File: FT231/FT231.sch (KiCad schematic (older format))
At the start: 19 parts, among them J1 USB_B_Micro, J2 Conn_01x03, J3 Conn_01x03, J4 Conn_01x06, U1 FT231XQ

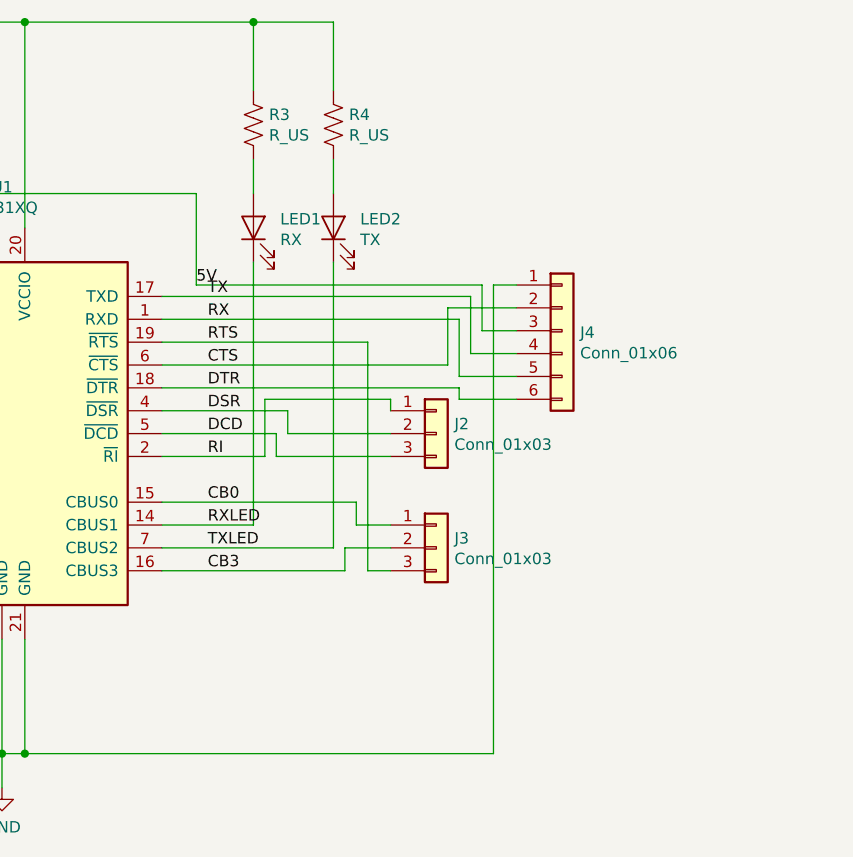
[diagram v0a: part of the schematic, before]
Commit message: Power LED Added
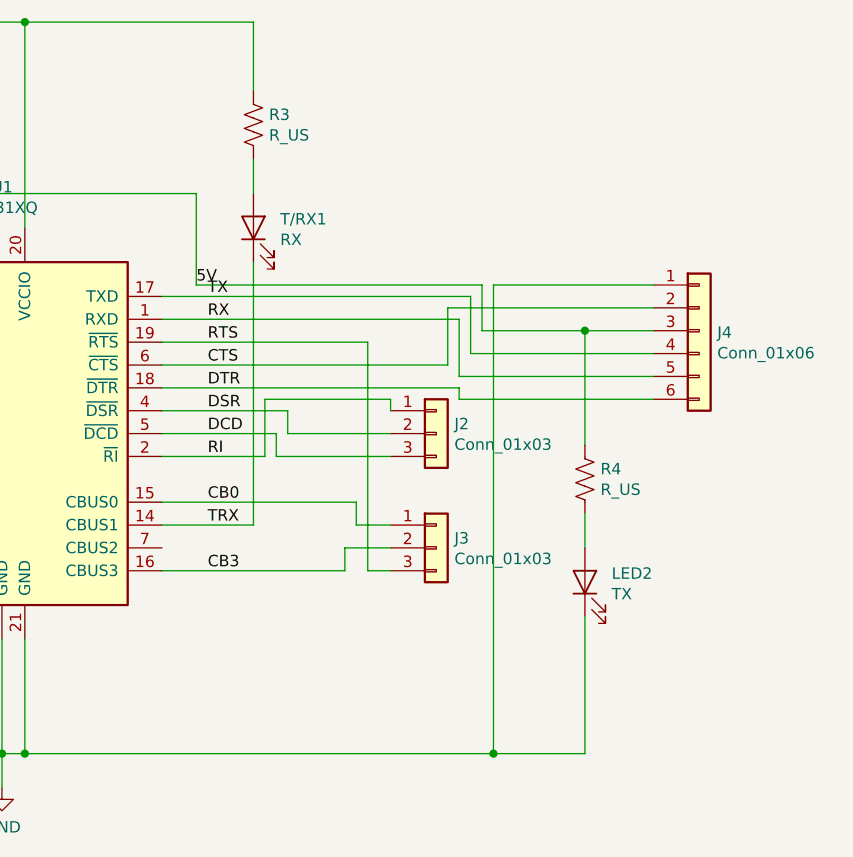
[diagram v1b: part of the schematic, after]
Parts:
- renumbered LED1 to T/RX1
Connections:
- net 5V: now also R4.1
- net GND: now also LED2.1 (K)
- net at C6.1, R3.1, U1.10 (3V3OUT)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: no longer R4.1
- net RXLED renamed TRX
- net TXLED: no longer names the net of U1.7 (CBUS2)
- net TXLED: no longer LED2.1 (K)
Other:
- moved on the sheet: J4, LED2, R4
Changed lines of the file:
@@
 L Device:R_US R4
 U 1 1 5D279F68
-P 6250 2150
-F 0 "R4" H 6318 2195 50  0000 L CNN
-F 1 "R_US" H 6318 2105 50  0000 L CNN
-F 2 "Resistor_SMD:R_0805_2012Metric_Pad1.15x1.40mm_HandSolder" V 6290 2140 50  0001 C CNN
-F 3 "~" H 6250 2150 50  0001 C CNN
-	1    6250 2150
+P 7350 3700
+F 0 "R4" H 7418 3745 50  0000 L CNN
+F 1 "R_US" H 7418 3655 50  0000 L CNN
+F 2 "Resistor_SMD:R_0805_2012Metric_Pad1.15x1.40mm_HandSolder" V 7390 3690 50  0001 C CNN
+F 3 "~" H 7350 3700 50  0001 C CNN
+	1    7350 3700
 	1    0    0    -1
 $EndComp
@@
 L Device:LED LED2
 U 1 1 5D27B0C2
-P 6250 2600
-F 0 "LED2" V 6288 2483 50  0000 R CNN
-F 1 "TX" V 6198 2483 50  0000 R CNN
-F 2 "LED_SMD:LED_0805_2012Metric_Castellated" H 6250 2600 50  0001 C CNN
-F 3 "~" H 6250 2600 50  0001 C CNN
-	1    6250 2600
+P 7350 4150
+F 0 "LED2" V 7388 4033 50  0000 R CNN
+F 1 "TX" V 7298 4033 50  0000 R CNN
+F 2 "LED_SMD:LED_0805_2012Metric_Castellated" H 7350 4150 50  0001 C CNN
+F 3 "~" H 7350 4150 50  0001 C CNN
+	1    7350 4150
 	0    -1   -1   0
 $EndComp
@@
 $EndComp
 $Comp
-L Device:LED LED1
+L Device:LED T/RX1
 U 1 1 5D282FEC
 P 5900 2600
-F 0 "LED1" V 5938 2483 50  0000 R CNN
+F 0 "T/RX1" V 5938 2483 50  0000 R CNN
 F 1 "RX" V 5848 2483 50  0000 R CNN
 F 2 "LED_SMD:LED_0805_2012Metric_Castellated" H 5900 2600 50  0001 C CNN
@@
 	5900 3900 5500 3900
 Wire Wire Line
-	6250 2300 6250 2450
-Wire Wire Line
-	6250 4000 5500 4000
+	7350 3850 7350 4000
 Wire Wire Line
 	4900 2600 4900 1700
@@
 	4900 1700 5900 1700
 Wire Wire Line
-	6250 1700 6250 2000
-Wire Wire Line
 	5900 2000 5900 1700
-Connection ~ 5900 1700
-Wire Wire Line
-	5900 1700 6250 1700
 Wire Wire Line
 	4100 3500 3950 3500
@@
 	3950 3800 3950 3500
 Connection ~ 3950 3500
-$Comp
-L Connector:USB_B_Micro J1
-U 1 1 5D28C6B2
-P 1750 3200
-F 0 "J1" H 1806 3665 50  0000 C CNN
-F 1 "USB_B_Micro" H 1806 3575 50  0000 C CNN
-F 2 "Connector_USB:USB_Micro-B_Molex_47346-0001" H 1900 3150 50  0001 C CNN
-F 3 "~" H 1900 3150 50  0001 C CNN
-	1    1750 3200
-	1    0    0    -1
-$EndComp
 $Comp
 L Device:R_US R1
@@
 $EndComp
 Wire Wire Line
-	2050 3000 2050 2450
-Wire Wire Line
-	2050 2450 2200 2450
-Wire Wire Line
 	4700 2450 4700 2600
 $Comp
@@
 	4050 3300 4100 3300
 Wire Wire Line
-	2050 3300 2700 3300
-Wire Wire Line
 	2750 3300 2750 3350
 Wire Wire Line
 	2750 3350 2850 3350
-Wire Wire Line
-	2050 3200 2500 3200
 Wire Wire Line
 	2500 3550 2500 3200
@@
 	2500 4900 2700 4900
 Connection ~ 2700 4900
-Wire Wire Line
-	1750 4900 2200 4900
 Connection ~ 2500 4900
-Wire Wire Line
-	1650 4900 1750 4900
-Connection ~ 1750 4900
 $Comp
 L Device:C C1
@@
 	2200 3850 2200 4900
 Wire Wire Line
-	1750 3600 1750 4900
-Wire Wire Line
-	1650 3600 1650 4900
-Wire Wire Line
 	4700 4400 4700 4900
 Wire Wire Line
@@
 L Connector_Generic:Conn_01x06 J4
 U 1 1 5D2E3C24
-P 7250 3050
-F 0 "J4" H 7329 3042 50  0000 L CNN
-F 1 "Conn_01x06" H 7329 2952 50  0000 L CNN
-F 2 "Connector_PinHeader_2.54mm:PinHeader_1x06_P2.54mm_Horizontal" H 7250 3050 50  0001 C CNN
-F 3 "~" H 7250 3050 50  0001 C CNN
-	1    7250 3050
+P 7850 3050
+F 0 "J4" H 7929 3042 50  0000 L CNN
+F 1 "Conn_01x06" H 7929 2952 50  0000 L CNN
+F 2 "Connector_PinHeader_2.54mm:PinHeader_1x06_P2.54mm_Horizontal" H 7850 3050 50  0001 C CNN
+F 3 "~" H 7850 3050 50  0001 C CNN
+	1    7850 3050
 	1    0    0    -1
 $EndComp
@@
 	5500 3200 6750 3200
 Wire Wire Line
-	6750 2950 7050 2950
-Wire Wire Line
-	6900 3050 7050 3050
-Wire Wire Line
-	6850 3150 7050 3150
-Wire Wire Line
-	6800 3250 7050 3250
-Wire Wire Line
-	6800 3350 7050 3350
-Wire Wire Line
-	7050 2850 6950 2850
+	6750 2950 7650 2950
+Wire Wire Line
+	6900 3050 7350 3050
+Wire Wire Line
+	6850 3150 7650 3150
+Wire Wire Line
+	6800 3250 7650 3250
+Wire Wire Line
+	6800 3350 7650 3350
+Wire Wire Line
+	7650 2850 6950 2850
 Wire Wire Line
 	6950 2850 6950 4900
@@
 Wire Wire Line
 	5900 2750 5900 3900
-Wire Wire Line
-	6250 2750 6250 4000
 $Comp
 L Connector_Generic:Conn_01x03 J3
@@
 CB0
 Text Label 5700 3900 0    50   ~ 0
-RXLED
-Text Label 5700 4000 0    50   ~ 0
-TXLED
+TRX
 Text Label 5700 4100 0    50   ~ 0
 CB3
+Connection ~ 1750 4900
+Wire Wire Line
+	1750 4900 2200 4900
+Wire Wire Line
+	1650 4900 1750 4900
+Wire Wire Line
+	2050 2450 2200 2450
+Wire Wire Line
+	1650 3600 1650 4900
+Wire Wire Line
+	1750 3600 1750 4900
+Wire Wire Line
+	2050 3200 2500 3200
+Wire Wire Line
+	2050 3300 2700 3300
+Wire Wire Line
+	2050 3000 2050 2450
+$Comp
+L Connector:USB_B_Micro J1
+U 1 1 5D28C6B2
+P 1750 3200
+F 0 "J1" H 1806 3665 50  0000 C CNN
+F 1 "USB_B_Micro" H 1806 3575 50  0000 C CNN
+F 2 "Connector_USB:USB_Micro-B_Molex_47346-0001" H 1900 3150 50  0001 C CNN
+F 3 "~" H 1900 3150 50  0001 C CNN
+	1    1750 3200
+	1    0    0    -1
+$EndComp
+Wire Wire Line
+	7350 3550 7350 3050
+Connection ~ 7350 3050
+Wire Wire Line
+	7350 3050 7650 3050
+Wire Wire Line
+	7350 4300 7350 4900
+Wire Wire Line
+	7350 4900 6950 4900
+Connection ~ 6950 4900
 $EndSCHEMATC

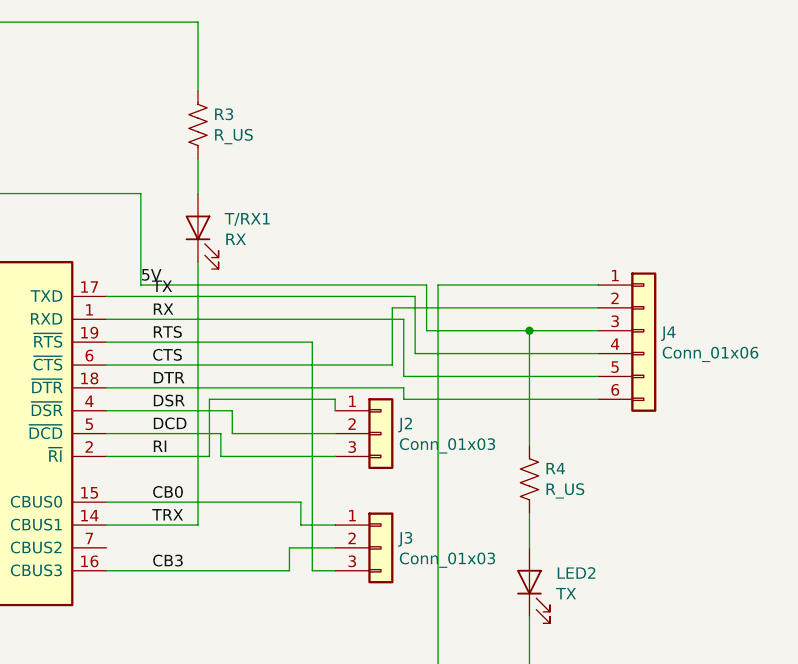
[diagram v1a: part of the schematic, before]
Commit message: Power LED edited
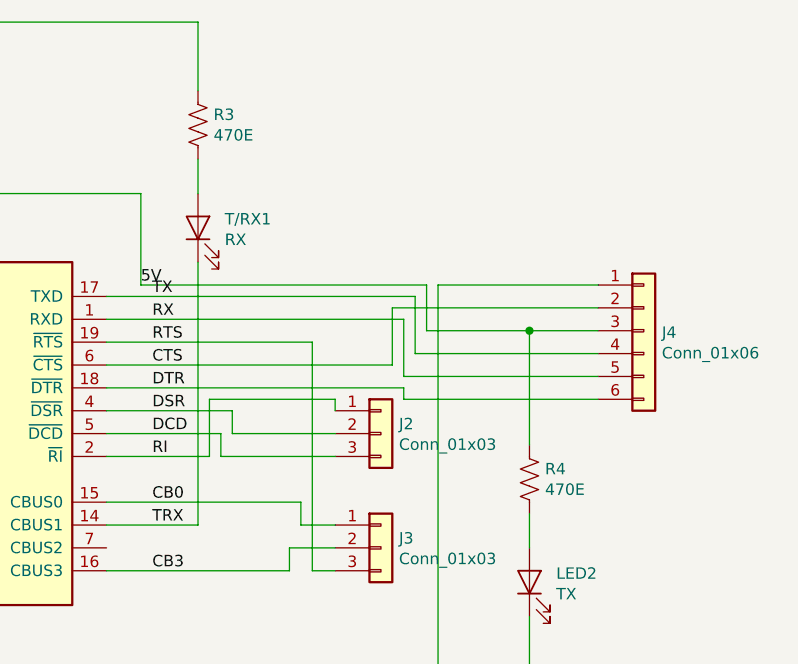
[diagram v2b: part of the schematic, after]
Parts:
- R3, R4: value R_US -> 470E
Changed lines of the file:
@@
-$EndComp
-$Comp
-L Device:R_US R4
-U 1 1 5D279F68
-P 7350 3700
-F 0 "R4" H 7418 3745 50  0000 L CNN
-F 1 "R_US" H 7418 3655 50  0000 L CNN
-F 2 "Resistor_SMD:R_0805_2012Metric_Pad1.15x1.40mm_HandSolder" V 7390 3690 50  0001 C CNN
-F 3 "~" H 7350 3700 50  0001 C CNN
-	1    7350 3700
-	1    0    0    -1
 $EndComp
 $Comp
@@
 	4800 4900 4700 4900
 $Comp
-L Device:LED LED2
-U 1 1 5D27B0C2
-P 7350 4150
-F 0 "LED2" V 7388 4033 50  0000 R CNN
-F 1 "TX" V 7298 4033 50  0000 R CNN
-F 2 "LED_SMD:LED_0805_2012Metric_Castellated" H 7350 4150 50  0001 C CNN
-F 3 "~" H 7350 4150 50  0001 C CNN
-	1    7350 4150
-	0    -1   -1   0
-$EndComp
-$Comp
 L Device:R_US R3
 U 1 1 5D282FE6
 P 5900 2150
 F 0 "R3" H 5968 2195 50  0000 L CNN
-F 1 "R_US" H 5968 2105 50  0000 L CNN
+F 1 "470E" H 5968 2105 50  0000 L CNN
 F 2 "Resistor_SMD:R_0805_2012Metric_Pad1.15x1.40mm_HandSolder" V 5940 2140 50  0001 C CNN
 F 3 "~" H 5900 2150 50  0001 C CNN
 	1    5900 2150
 	1    0    0    -1
-$EndComp
-$Comp
-L Device:LED T/RX1
-U 1 1 5D282FEC
-P 5900 2600
-F 0 "T/RX1" V 5938 2483 50  0000 R CNN
-F 1 "RX" V 5848 2483 50  0000 R CNN
-F 2 "LED_SMD:LED_0805_2012Metric_Castellated" H 5900 2600 50  0001 C CNN
-F 3 "~" H 5900 2600 50  0001 C CNN
-	1    5900 2600
-	0    -1   -1   0
 $EndComp
 Wire Wire Line
@@
 	7350 4900 6950 4900
 Connection ~ 6950 4900
+$Comp
+L Device:LED T/RX1
+U 1 1 5D282FEC
+P 5900 2600
+F 0 "T/RX1" V 5938 2483 50  0000 R CNN
+F 1 "RX" V 5848 2483 50  0000 R CNN
+F 2 "LED_SMD:LED_0805_2012Metric_Castellated" H 5900 2600 50  0001 C CNN
+F 3 "~" H 5900 2600 50  0001 C CNN
+	1    5900 2600
+	0    -1   -1   0
+$EndComp
+$Comp
+L Device:R_US R4
+U 1 1 5D279F68
+P 7350 3700
+F 0 "R4" H 7418 3745 50  0000 L CNN
+F 1 "470E" H 7418 3655 50  0000 L CNN
+F 2 "Resistor_SMD:R_0805_2012Metric_Pad1.15x1.40mm_HandSolder" V 7390 3690 50  0001 C CNN
+F 3 "~" H 7350 3700 50  0001 C CNN
+	1    7350 3700
+	1    0    0    -1
+$EndComp
+$Comp
+L Device:LED LED2
+U 1 1 5D27B0C2
+P 7350 4150
+F 0 "LED2" V 7388 4033 50  0000 R CNN
+F 1 "TX" V 7298 4033 50  0000 R CNN
+F 2 "LED_SMD:LED_0805_2012Metric_Castellated" H 7350 4150 50  0001 C CNN
+F 3 "~" H 7350 4150 50  0001 C CNN
+	1    7350 4150
+	0    -1   -1   0
+$EndComp
 $EndSCHEMATC

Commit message: Page Settings Updated
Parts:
- FB1: value Ferrite_Bead -> 40E@100MHz
- LED2: value TX -> RED
- T/RX1: value RX -> GREEN
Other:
- moved on the sheet: C1, C2, C3, C4, C5, C6, FB1, J1, J2, J3, J4, JP1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

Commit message: Part Numbers Added
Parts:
- removed JP1: SolderJumper_2_Open, Jumper:SolderJumper-2_P1.3mm_Bridged_RoundedPad1.0x1.5mm, symbol Jumper:SolderJumper_2_Open
- added JP1: SolderJumper_2_Bridged, Jumper:SolderJumper-2_P1.3mm_Bridged_RoundedPad1.0x1.5mm, symbol Jumper:SolderJumper_2_Bridged
- added R5: 680E, Resistor_SMD:R_0603_1608Metric, symbol Device:R_US
- added TX1: GREEN, LED_SMD:LED_0603_1608Metric, symbol Device:LED
- C1: footprint Capacitor_SMD:C_0805_2012Metric_Pad1.15x1.40mm_HandSolder -> Capacitor_SMD:C_0603_1608Metric; Part (none) -> C100042
- C2, C3: footprint Capacitor_SMD:C_0805_2012Metric_Pad1.15x1.40mm_HandSolder -> Capacitor_SMD:C_0603_1608Metric; Part (none) -> C105622
- C4, C6: footprint Capacitor_SMD:C_0805_2012Metric_Pad1.15x1.40mm_HandSolder -> Capacitor_SMD:C_0603_1608Metric; Part (none) -> C42998
- C5: Part (none) -> C87998
- FB1: footprint Inductor_SMD:L_0805_2012Metric_Pad1.15x1.40mm_HandSolder -> Inductor_SMD:L_0603_1608Metric; Part (none) -> C53139
- PWR1: renamed from LED2; footprint LED_SMD:LED_0805_2012Metric_Castellated -> LED_SMD:LED_0603_1608Metric; Part (none) -> C118330
- R1, R2: footprint Resistor_SMD:R_0805_2012Metric_Pad1.15x1.40mm_HandSolder -> Resistor_SMD:R_0603_1608Metric; Part (none) -> C325726
- R3, R4: value 470E -> 680E; footprint Resistor_SMD:R_0805_2012Metric_Pad1.15x1.40mm_HandSolder -> Resistor_SMD:R_0603_1608Metric; Part (none) -> C269441
- RX1: renamed from T/RX1; footprint LED_SMD:LED_0805_2012Metric_Castellated -> LED_SMD:LED_0603_1608Metric; Part (none) -> C205443
- U1: Part (none) -> 757-0045
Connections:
- net at C6.1, R3.1, U1.10 (3V3OUT)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: now also R5.1
- net at C1.1, J1.1 (VBUS): now also JP1.1 (A)
- net TXLED: now reaches U1.7 (CBUS2)
- net TXLED: now also TX1.1 (K)
- net at FB1.2: now also JP1.2 (B)
- net TRX renamed RXLED
- new net: R5.2, TX1.2 (A)
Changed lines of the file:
@@
 F 0 "C6" H 3475 2850 50  0000 L CNN
 F 1 "100nF" H 3475 2650 50  0000 L CNN
-F 2 "Capacitor_SMD:C_0805_2012Metric_Pad1.15x1.40mm_HandSolder" H 3463 2600 50  0001 C CNN
+F 2 "Capacitor_SMD:C_0603_1608Metric" H 3463 2600 50  0001 C CNN
 F 3 "~" H 3425 2750 50  0001 C CNN
+F 4 "C42998" H 3425 2750 50  0001 C CNN "Part"
 	1    3425 2750
 	1    0    0    -1
@@
 F 2 "Capacitor_SMD:C_0805_2012Metric_Pad1.15x1.40mm_HandSolder" H 3113 2600 50  0001 C CNN
 F 3 "~" H 3075 2750 50  0001 C CNN
+F 4 "C87998" H 3075 2750 50  0001 C CNN "Part"
 	1    3075 2750
 	1    0    0    -1
@@
 P 5375 975
 F 0 "R3" H 5443 1020 50  0000 L CNN
-F 1 "470E" H 5443 930 50  0000 L CNN
-F 2 "Resistor_SMD:R_0805_2012Metric_Pad1.15x1.40mm_HandSolder" V 5415 965 50  0001 C CNN
+F 1 "680E" H 5443 930 50  0000 L CNN
+F 2 "Resistor_SMD:R_0603_1608Metric" V 5415 965 50  0001 C CNN
 F 3 "~" H 5375 975 50  0001 C CNN
+F 4 "C269441" H 5375 975 50  0001 C CNN "Part"
 	1    5375 975
 	1    0    0    -1
@@
 F 0 "R1" V 2678 2000 50  0000 C CNN
 F 1 "27e" V 2588 2000 50  0000 C CNN
-F 2 "Resistor_SMD:R_0805_2012Metric_Pad1.15x1.40mm_HandSolder" V 2515 1990 50  0001 C CNN
+F 2 "Resistor_SMD:R_0603_1608Metric" V 2515 1990 50  0001 C CNN
 F 3 "~" H 2475 2000 50  0001 C CNN
+F 4 "C325726" V 2475 2000 50  0001 C CNN "Part"
 	1    2475 2000
 	0    -1   -1   0
@@
 F 0 "R2" V 2678 2150 50  0000 C CNN
 F 1 "27e" V 2588 2150 50  0000 C CNN
-F 2 "Resistor_SMD:R_0805_2012Metric_Pad1.15x1.40mm_HandSolder" V 2515 2140 50  0001 C CNN
+F 2 "Resistor_SMD:R_0603_1608Metric" V 2515 2140 50  0001 C CNN
 F 3 "~" H 2475 2150 50  0001 C CNN
+F 4 "C325726" V 2475 2150 50  0001 C CNN "Part"
 	1    2475 2150
 	0    1    1    0
@@
 F 0 "C3" H 2250 2600 50  0000 L CNN
 F 1 "47pF" H 2250 2400 50  0000 L CNN
-F 2 "Capacitor_SMD:C_0805_2012Metric_Pad1.15x1.40mm_HandSolder" H 2213 2350 50  0001 C CNN
+F 2 "Capacitor_SMD:C_0603_1608Metric" H 2213 2350 50  0001 C CNN
 F 3 "~" H 2175 2500 50  0001 C CNN
+F 4 "C105622" H 2175 2500 50  0001 C CNN "Part"
 	1    2175 2500
 	1    0    0    -1
@@
 F 0 "C2" H 2025 2600 50  0000 L CNN
 F 1 "47pF" H 2025 2400 50  0000 L CNN
-F 2 "Capacitor_SMD:C_0805_2012Metric_Pad1.15x1.40mm_HandSolder" H 2013 2350 50  0001 C CNN
+F 2 "Capacitor_SMD:C_0603_1608Metric" H 2013 2350 50  0001 C CNN
 F 3 "~" H 1975 2500 50  0001 C CNN
+F 4 "C105622" H 1975 2500 50  0001 C CNN "Part"
 	1    1975 2500
 	-1   0    0    -1
@@
 F 0 "C4" H 2775 2850 50  0000 R CNN
 F 1 "100nF" H 2775 2650 50  0000 R CNN
-F 2 "Capacitor_SMD:C_0805_2012Metric_Pad1.15x1.40mm_HandSolder" H 2863 2600 50  0001 C CNN
+F 2 "Capacitor_SMD:C_0603_1608Metric" H 2863 2600 50  0001 C CNN
 F 3 "~" H 2825 2750 50  0001 C CNN
+F 4 "C42998" H 2825 2750 50  0001 C CNN "Part"
 	1    2825 2750
 	1    0    0    -1
@@
 F 0 "C1" H 1600 2600 50  0000 R CNN
 F 1 "10nF" H 1600 2400 50  0000 R CNN
-F 2 "Capacitor_SMD:C_0805_2012Metric_Pad1.15x1.40mm_HandSolder" H 1713 2350 50  0001 C CNN
+F 2 "Capacitor_SMD:C_0603_1608Metric" H 1713 2350 50  0001 C CNN
 F 3 "~" H 1675 2500 50  0001 C CNN
+F 4 "C100042" H 1675 2500 50  0001 C CNN "Part"
 	1    1675 2500
 	1    0    0    -1
@@
 F 0 "FB1" V 2053 1250 50  0000 C CNN
 F 1 "40E@100MHz" V 2143 1250 50  0000 C CNN
-F 2 "Inductor_SMD:L_0805_2012Metric_Pad1.15x1.40mm_HandSolder" V 2255 1250 50  0001 C CNN
+F 2 "Inductor_SMD:L_0603_1608Metric" V 2255 1250 50  0001 C CNN
 F 3 "~" H 2325 1250 50  0001 C CNN
+F 4 "C53139" V 2325 1250 50  0001 C CNN "Part"
 	1    2325 1250
 	0    1    1    0
@@
 Text Label 2925 2150 0    50   ~ 0
 uD-
-$Comp
-L Jumper:SolderJumper_2_Open JP1
-U 1 1 5D2E73C8
-P 1925 1250
-F 0 "JP1" H 1925 1350 50  0000 C CNN
-F 1 "SolderJumper_2_Open" H 1925 1363 50  0001 C CNN
-F 2 "Jumper:SolderJumper-2_P1.3mm_Bridged_RoundedPad1.0x1.5mm" H 1925 1250 50  0001 C CNN
-F 3 "~" H 1925 1250 50  0001 C CNN
-	1    1925 1250
-	1    0    0    -1
-$EndComp
 Wire Wire Line
 	2075 1250 2175 1250
@@
 F 2 "Package_DFN_QFN:QFN-20-1EP_4x4mm_P0.5mm_EP2.5x2.5mm" H 4775 1450 50  0001 C CNN
 F 3 "http://www.ftdichip.com/Products/ICs/FT231X.html" H 4275 2300 50  0001 C CNN
+F 4 "757-0045" H 4275 2300 50  0001 C CNN "Part"
 	1    4275 2300
 	1    0    0    -1
@@
 CB0
 Text Label 5175 2700 0    50   ~ 0
-TRX
+RXLED
 Text Label 5175 2900 0    50   ~ 0
 CB3
@@
 Connection ~ 6425 3700
 $Comp
-L Device:LED T/RX1
+L Device:LED RX1
 U 1 1 5D282FEC
 P 5375 1400
-F 0 "T/RX1" V 5413 1283 50  0000 R CNN
+F 0 "RX1" V 5413 1283 50  0000 R CNN
 F 1 "GREEN" V 5323 1283 50  0000 R CNN
-F 2 "LED_SMD:LED_0805_2012Metric_Castellated" H 5375 1400 50  0001 C CNN
+F 2 "LED_SMD:LED_0603_1608Metric" H 5375 1400 50  0001 C CNN
 F 3 "~" H 5375 1400 50  0001 C CNN
+F 4 "C205443" V 5375 1400 50  0001 C CNN "Part"
 	1    5375 1400
 	0    -1   -1   0
@@
 P 6825 2500
 F 0 "R4" H 6893 2545 50  0000 L CNN
-F 1 "470E" H 6893 2455 50  0000 L CNN
-F 2 "Resistor_SMD:R_0805_2012Metric_Pad1.15x1.40mm_HandSolder" V 6865 2490 50  0001 C CNN
+F 1 "680E" H 6893 2455 50  0000 L CNN
+F 2 "Resistor_SMD:R_0603_1608Metric" V 6865 2490 50  0001 C CNN
 F 3 "~" H 6825 2500 50  0001 C CNN
+F 4 "C269441" H 6825 2500 50  0001 C CNN "Part"
 	1    6825 2500
 	1    0    0    -1
 $EndComp
 $Comp
-L Device:LED LED2
+L Device:LED PWR1
 U 1 1 5D27B0C2
 P 6825 2950
-F 0 "LED2" V 6863 2833 50  0000 R CNN
+F 0 "PWR1" V 6863 2833 50  0000 R CNN
 F 1 "RED" V 6773 2833 50  0000 R CNN
-F 2 "LED_SMD:LED_0805_2012Metric_Castellated" H 6825 2950 50  0001 C CNN
+F 2 "LED_SMD:LED_0603_1608Metric" H 6825 2950 50  0001 C CNN
 F 3 "~" H 6825 2950 50  0001 C CNN
+F 4 "C118330" V 6825 2950 50  0001 C CNN "Part"
 	1    6825 2950
 	0    -1   -1   0
 $EndComp
+$Comp
+L Device:R_US R5
+U 1 1 5E31B458
+P 5850 975
+F 0 "R5" H 5918 1020 50  0000 L CNN
+F 1 "680E" H 5918 930 50  0000 L CNN
+F 2 "Resistor_SMD:R_0603_1608Metric" V 5890 965 50  0001 C CNN
+F 3 "~" H 5850 975 50  0001 C CNN
+F 4 "C269441" H 5850 975 50  0001 C CNN "Part"
+	1    5850 975
+	1    0    0    -1
+$EndComp
+Wire Wire Line
+	5850 1125 5850 1250
+Wire Wire Line
+	5850 825  5850 725
+$Comp
+L Device:LED TX1
+U 1 1 5E31B461
+P 5850 1400
+F 0 "TX1" V 5888 1283 50  0000 R CNN
+F 1 "GREEN" V 5798 1283 50  0000 R CNN
+F 2 "LED_SMD:LED_0603_1608Metric" H 5850 1400 50  0001 C CNN
+F 3 "~" H 5850 1400 50  0001 C CNN
+F 4 "C205443" V 5850 1400 50  0001 C CNN "Part"
+	1    5850 1400
+	0    -1   -1   0
+$EndComp
+Wire Wire Line
+	5850 725  5375 725
+Connection ~ 5375 725
+Wire Wire Line
+	4975 2800 5725 2800
+Wire Wire Line
+	5725 2800 5725 1625
+Wire Wire Line
+	5725 1625 5850 1625
+Wire Wire Line
+	5850 1625 5850 1550
+Text Label 5175 2800 0    50   ~ 0
+TXLED
+$Comp
+L Jumper:SolderJumper_2_Bridged JP1
+U 1 1 5E33F873
+P 1925 1250
+F 0 "JP1" H 1925 1453 50  0000 C CNN
+F 1 "SolderJumper_2_Bridged" H 1925 1363 50  0000 C CNN
+F 2 "Jumper:SolderJumper-2_P1.3mm_Bridged_RoundedPad1.0x1.5mm" H 1925 1250 50  0001 C CNN
+F 3 "~" H 1925 1250 50  0001 C CNN
+	1    1925 1250
+	1    0    0    -1
+$EndComp
 $EndSCHEMATC
